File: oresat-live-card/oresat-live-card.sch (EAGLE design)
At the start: 281 parts, among them J1 ORESAT-DEBUG-CONNECTOR-CARD, J100 DM3BT-DSF-PEJS, J102 FTSH-105-XX-X-DV-K, J2 SM06B-SRSS-TB(LF)(SN), J4 TFM-120-01-L-D-RA, Q1 MMBT2907, Q2 PMV45EN, Q3 DMP2240UDM, Q4 PMV45EN, Q5 MOSFET-PCH-SOT23-6, Q6 MOSFET-PCH-SOT23-6, U1 RCLAMP0504FB, U10 TLVH431, U11 TCAN330, U12 MIC842LYC5, U13 MIC842LYC5, U14 MAX4211FETE, U15 TPS62112, U16 MAX7310ATE, U17 25AAXX, U18 RCLAMP0504FB, U2 TPS2051CDBVR, U3 THGBMJG7C2LBAU8, U4 SN74LVC1G07DCK, U7 OSD3358-512M-BSM, Y1 24MHz, Y2 ABS07-32.768KHZ-T

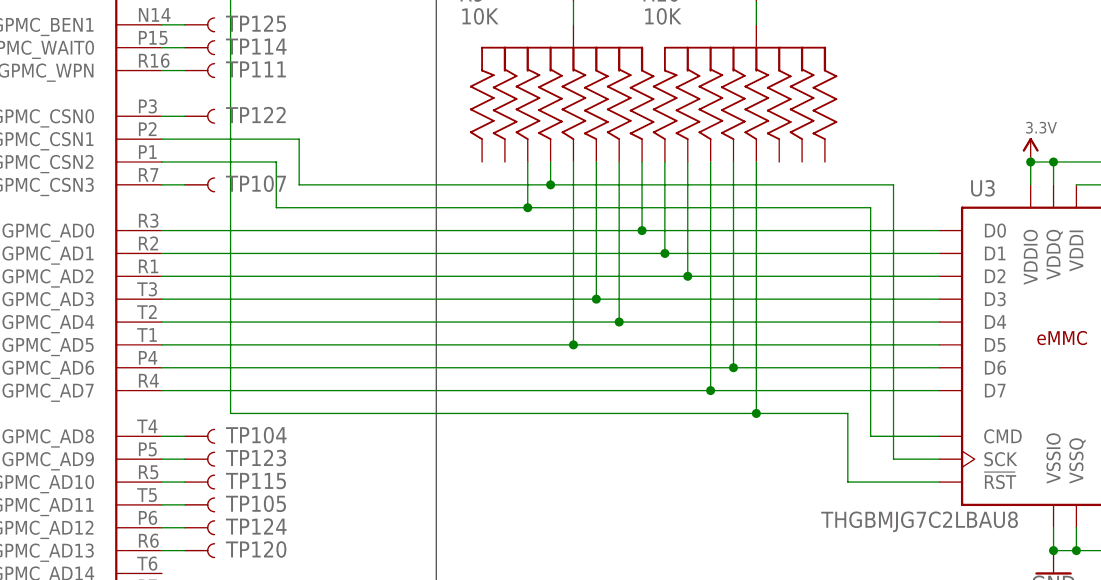
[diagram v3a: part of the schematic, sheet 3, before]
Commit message: relocated emmc pullups and reworked the assigned pins for easier layout
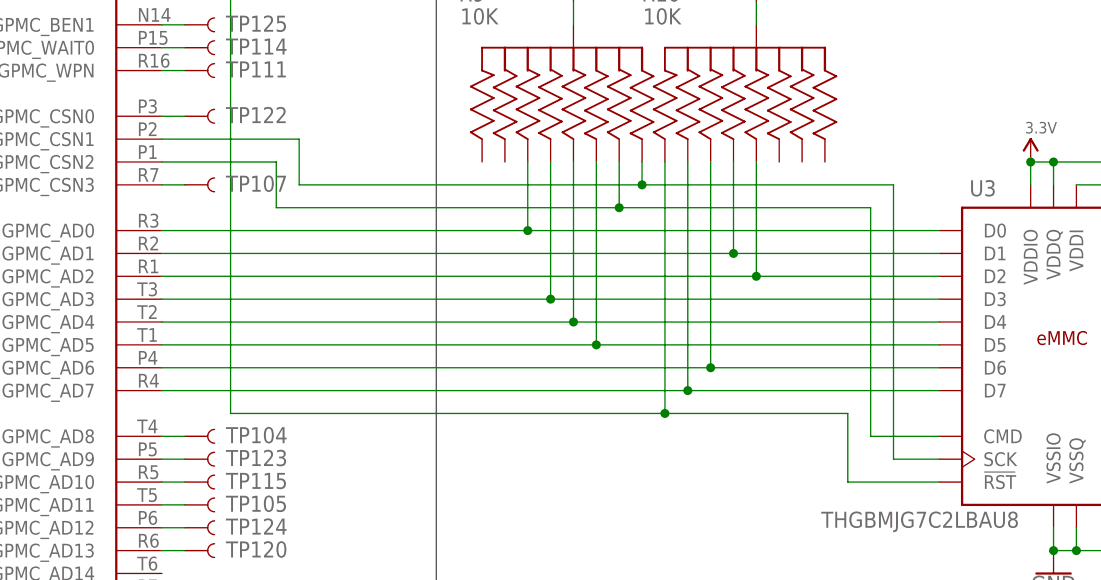
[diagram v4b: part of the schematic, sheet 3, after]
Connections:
- net N$641: now also R9.22; no longer R9.66
- net N$642: now also R10.88; no longer R10.11
- net N$643: now also R10.33; no longer R10.99
- net N$644: now also R9.88; no longer R9.77
- net N$645: now also R9.33; no longer R9.44
- net N$646: now also R9.77; no longer R9.33
- net N$647: now also R10.22; no longer R10.88
- net N$648: now also R10.99; no longer R10.22
- net N$649: now also R9.44; no longer R9.22
- net N$651: now also R9.66; no longer R9.88
- net N$652: now also R10.11; no longer R10.33
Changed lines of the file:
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@@
 <?xml version="1.0" encoding="utf-8"?>
 <!DOCTYPE eagle SYSTEM "eagle.dtd">
-<eagle version="9.6.1">
+<eagle version="9.6.2">
 <drawing>
 <settings>
@@
 <pinref part="U7" gate="C" pin="GPMC_AD0"/>
 <pinref part="U3" gate="U" pin="D0"/>
-<wire x1="350.52" y1="345.44" x2="403.86" y2="345.44" width="0.1524" layer="91"/>
-<wire x1="403.86" y1="345.44" x2="436.88" y2="345.44" width="0.1524" layer="91"/>
-<wire x1="403.86" y1="345.44" x2="403.86" y2="353.06" width="0.1524" layer="91"/>
-<junction x="403.86" y="345.44"/>
-<pinref part="R9" gate="A" pin="66"/>
+<wire x1="350.52" y1="345.44" x2="391.16" y2="345.44" width="0.1524" layer="91"/>
+<pinref part="R9" gate="A" pin="22"/>
+<wire x1="391.16" y1="345.44" x2="436.88" y2="345.44" width="0.1524" layer="91"/>
+<wire x1="391.16" y1="353.06" x2="391.16" y2="345.44" width="0.1524" layer="91"/>
+<junction x="391.16" y="345.44"/>
 </segment>
 </net>
@@
 <pinref part="U7" gate="C" pin="GPMC_AD1"/>
 <pinref part="U3" gate="U" pin="D1"/>
-<wire x1="350.52" y1="342.9" x2="406.4" y2="342.9" width="0.1524" layer="91"/>
-<wire x1="406.4" y1="342.9" x2="436.88" y2="342.9" width="0.1524" layer="91"/>
-<wire x1="406.4" y1="342.9" x2="406.4" y2="353.06" width="0.1524" layer="91"/>
-<junction x="406.4" y="342.9"/>
-<pinref part="R10" gate="A" pin="11"/>
+<wire x1="350.52" y1="342.9" x2="414.02" y2="342.9" width="0.1524" layer="91"/>
+<pinref part="R10" gate="A" pin="88"/>
+<wire x1="414.02" y1="342.9" x2="436.88" y2="342.9" width="0.1524" layer="91"/>
+<wire x1="414.02" y1="353.06" x2="414.02" y2="342.9" width="0.1524" layer="91"/>
+<junction x="414.02" y="342.9"/>
 </segment>
 </net>
@@
 <pinref part="U3" gate="U" pin="D2"/>
 <pinref part="U7" gate="C" pin="GPMC_AD2"/>
-<wire x1="436.88" y1="340.36" x2="408.94" y2="340.36" width="0.1524" layer="91"/>
-<wire x1="408.94" y1="340.36" x2="350.52" y2="340.36" width="0.1524" layer="91"/>
-<wire x1="408.94" y1="340.36" x2="408.94" y2="353.06" width="0.1524" layer="91"/>
-<junction x="408.94" y="340.36"/>
-<pinref part="R10" gate="A" pin="99"/>
+<wire x1="436.88" y1="340.36" x2="416.56" y2="340.36" width="0.1524" layer="91"/>
+<pinref part="R10" gate="A" pin="33"/>
+<wire x1="416.56" y1="340.36" x2="350.52" y2="340.36" width="0.1524" layer="91"/>
+<wire x1="416.56" y1="353.06" x2="416.56" y2="340.36" width="0.1524" layer="91"/>
+<junction x="416.56" y="340.36"/>
 </segment>
 </net>
@@
 <pinref part="U7" gate="C" pin="GPMC_AD3"/>
 <pinref part="U3" gate="U" pin="D3"/>
-<wire x1="350.52" y1="337.82" x2="398.78" y2="337.82" width="0.1524" layer="91"/>
-<wire x1="398.78" y1="337.82" x2="436.88" y2="337.82" width="0.1524" layer="91"/>
-<wire x1="398.78" y1="337.82" x2="398.78" y2="353.06" width="0.1524" layer="91"/>
-<junction x="398.78" y="337.82"/>
-<pinref part="R9" gate="A" pin="77"/>
+<wire x1="350.52" y1="337.82" x2="393.7" y2="337.82" width="0.1524" layer="91"/>
+<pinref part="R9" gate="A" pin="88"/>
+<wire x1="393.7" y1="337.82" x2="436.88" y2="337.82" width="0.1524" layer="91"/>
+<wire x1="393.7" y1="353.06" x2="393.7" y2="337.82" width="0.1524" layer="91"/>
+<junction x="393.7" y="337.82"/>
 </segment>
 </net>
@@
 <pinref part="U3" gate="U" pin="D4"/>
 <pinref part="U7" gate="C" pin="GPMC_AD4"/>
-<wire x1="436.88" y1="335.28" x2="401.32" y2="335.28" width="0.1524" layer="91"/>
-<wire x1="401.32" y1="335.28" x2="350.52" y2="335.28" width="0.1524" layer="91"/>
-<wire x1="401.32" y1="335.28" x2="401.32" y2="353.06" width="0.1524" layer="91"/>
-<junction x="401.32" y="335.28"/>
-<pinref part="R9" gate="A" pin="44"/>
+<wire x1="436.88" y1="335.28" x2="396.24" y2="335.28" width="0.1524" layer="91"/>
+<pinref part="R9" gate="A" pin="33"/>
+<wire x1="396.24" y1="335.28" x2="350.52" y2="335.28" width="0.1524" layer="91"/>
+<wire x1="396.24" y1="353.06" x2="396.24" y2="335.28" width="0.1524" layer="91"/>
+<junction x="396.24" y="335.28"/>
 </segment>
 </net>
@@
 <pinref part="U3" gate="U" pin="D5"/>
 <pinref part="U7" gate="C" pin="GPMC_AD5"/>
-<wire x1="436.88" y1="332.74" x2="396.24" y2="332.74" width="0.1524" layer="91"/>
-<wire x1="396.24" y1="332.74" x2="350.52" y2="332.74" width="0.1524" layer="91"/>
-<wire x1="396.24" y1="332.74" x2="396.24" y2="353.06" width="0.1524" layer="91"/>
-<junction x="396.24" y="332.74"/>
-<pinref part="R9" gate="A" pin="33"/>
+<wire x1="436.88" y1="332.74" x2="398.78" y2="332.74" width="0.1524" layer="91"/>
+<pinref part="R9" gate="A" pin="77"/>
+<wire x1="398.78" y1="332.74" x2="350.52" y2="332.74" width="0.1524" layer="91"/>
+<wire x1="398.78" y1="353.06" x2="398.78" y2="332.74" width="0.1524" layer="91"/>
+<junction x="398.78" y="332.74"/>
 </segment>
 </net>
@@
 <pinref part="U7" gate="C" pin="GPMC_AD6"/>
 <pinref part="U3" gate="U" pin="D6"/>
-<wire x1="350.52" y1="330.2" x2="414.02" y2="330.2" width="0.1524" layer="91"/>
-<wire x1="414.02" y1="330.2" x2="436.88" y2="330.2" width="0.1524" layer="91"/>
-<wire x1="414.02" y1="330.2" x2="414.02" y2="353.06" width="0.1524" layer="91"/>
-<junction x="414.02" y="330.2"/>
-<pinref part="R10" gate="A" pin="88"/>
+<wire x1="350.52" y1="330.2" x2="411.48" y2="330.2" width="0.1524" layer="91"/>
+<pinref part="R10" gate="A" pin="22"/>
+<wire x1="411.48" y1="330.2" x2="436.88" y2="330.2" width="0.1524" layer="91"/>
+<wire x1="411.48" y1="353.06" x2="411.48" y2="330.2" width="0.1524" layer="91"/>
+<junction x="411.48" y="330.2"/>
 </segment>
 </net>
@@
 <pinref part="U3" gate="U" pin="D7"/>
 <pinref part="U7" gate="C" pin="GPMC_AD7"/>
-<wire x1="436.88" y1="327.66" x2="411.48" y2="327.66" width="0.1524" layer="91"/>
-<wire x1="411.48" y1="327.66" x2="350.52" y2="327.66" width="0.1524" layer="91"/>
-<wire x1="411.48" y1="353.06" x2="411.48" y2="327.66" width="0.1524" layer="91"/>
-<junction x="411.48" y="327.66"/>
-<pinref part="R10" gate="A" pin="22"/>
+<wire x1="436.88" y1="327.66" x2="408.94" y2="327.66" width="0.1524" layer="91"/>
+<pinref part="R10" gate="A" pin="99"/>
+<wire x1="408.94" y1="327.66" x2="350.52" y2="327.66" width="0.1524" layer="91"/>
+<wire x1="408.94" y1="353.06" x2="408.94" y2="327.66" width="0.1524" layer="91"/>
+<junction x="408.94" y="327.66"/>
 </segment>
 </net>
@@
 <wire x1="363.22" y1="353.06" x2="363.22" y2="347.98" width="0.1524" layer="91"/>
 <pinref part="U3" gate="U" pin="CMD"/>
-<wire x1="363.22" y1="347.98" x2="391.16" y2="347.98" width="0.1524" layer="91"/>
-<wire x1="391.16" y1="347.98" x2="429.26" y2="347.98" width="0.1524" layer="91"/>
+<wire x1="363.22" y1="347.98" x2="401.32" y2="347.98" width="0.1524" layer="91"/>
+<wire x1="401.32" y1="347.98" x2="429.26" y2="347.98" width="0.1524" layer="91"/>
 <wire x1="436.88" y1="322.58" x2="429.26" y2="322.58" width="0.1524" layer="91"/>
 <wire x1="429.26" y1="322.58" x2="429.26" y2="347.98" width="0.1524" layer="91"/>
-<wire x1="391.16" y1="347.98" x2="391.16" y2="353.06" width="0.1524" layer="91"/>
-<junction x="391.16" y="347.98"/>
-<pinref part="R9" gate="A" pin="22"/>
+<pinref part="R9" gate="A" pin="44"/>
+<wire x1="401.32" y1="353.06" x2="401.32" y2="347.98" width="0.1524" layer="91"/>
+<junction x="401.32" y="347.98"/>
 </segment>
 </net>
@@
 <wire x1="350.52" y1="355.6" x2="365.76" y2="355.6" width="0.1524" layer="91"/>
 <wire x1="365.76" y1="355.6" x2="365.76" y2="350.52" width="0.1524" layer="91"/>
-<wire x1="365.76" y1="350.52" x2="393.7" y2="350.52" width="0.1524" layer="91"/>
-<wire x1="393.7" y1="350.52" x2="431.8" y2="350.52" width="0.1524" layer="91"/>
-<wire x1="393.7" y1="350.52" x2="393.7" y2="353.06" width="0.1524" layer="91"/>
-<junction x="393.7" y="350.52"/>
-<pinref part="R9" gate="A" pin="88"/>
+<wire x1="365.76" y1="350.52" x2="403.86" y2="350.52" width="0.1524" layer="91"/>
+<pinref part="R9" gate="A" pin="66"/>
+<wire x1="403.86" y1="350.52" x2="431.8" y2="350.52" width="0.1524" layer="91"/>
+<wire x1="403.86" y1="353.06" x2="403.86" y2="350.52" width="0.1524" layer="91"/>
+<junction x="403.86" y="350.52"/>
 </segment>
 </net>
@@
 <wire x1="350.52" y1="391.16" x2="358.14" y2="391.16" width="0.1524" layer="91"/>
 <wire x1="358.14" y1="391.16" x2="358.14" y2="325.12" width="0.1524" layer="91"/>
-<wire x1="358.14" y1="325.12" x2="416.56" y2="325.12" width="0.1524" layer="91"/>
+<wire x1="358.14" y1="325.12" x2="406.4" y2="325.12" width="0.1524" layer="91"/>
 <pinref part="U3" gate="U" pin="!RST!"/>
-<wire x1="416.56" y1="325.12" x2="426.72" y2="325.12" width="0.1524" layer="91"/>
+<wire x1="406.4" y1="325.12" x2="426.72" y2="325.12" width="0.1524" layer="91"/>
 <wire x1="436.88" y1="317.5" x2="426.72" y2="317.5" width="0.1524" layer="91"/>
 <wire x1="426.72" y1="317.5" x2="426.72" y2="325.12" width="0.1524" layer="91"/>
-<wire x1="416.56" y1="353.06" x2="416.56" y2="325.12" width="0.1524" layer="91"/>
-<junction x="416.56" y="325.12"/>
-<pinref part="R10" gate="A" pin="33"/>
+<pinref part="R10" gate="A" pin="11"/>
+<wire x1="406.4" y1="353.06" x2="406.4" y2="325.12" width="0.1524" layer="91"/>
+<junction x="406.4" y="325.12"/>
 </segment>
 </net>

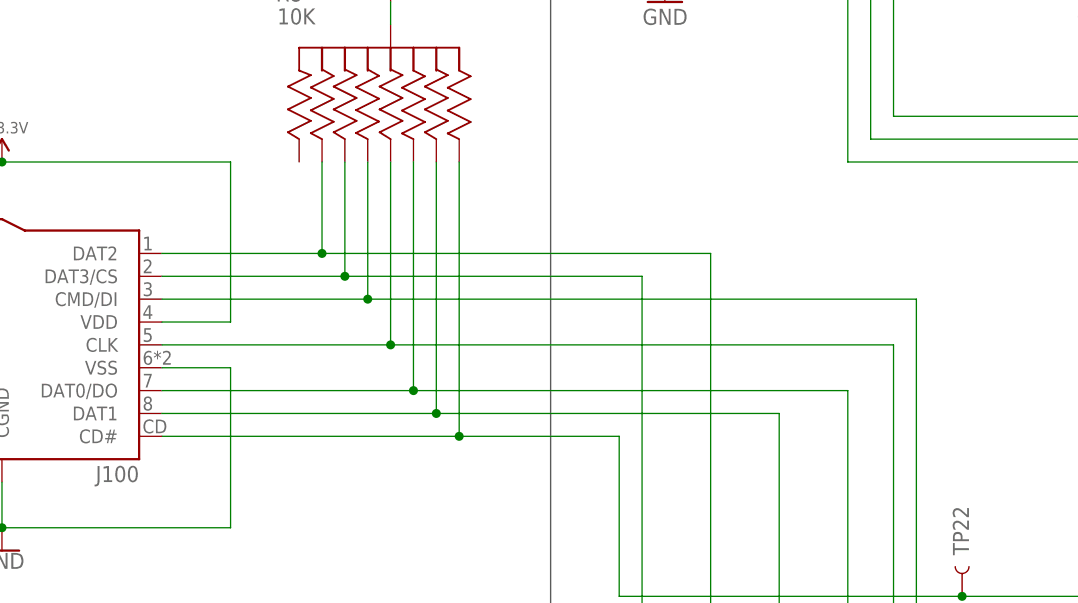
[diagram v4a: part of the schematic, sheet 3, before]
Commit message: routed sd data and reworked R8 pinout
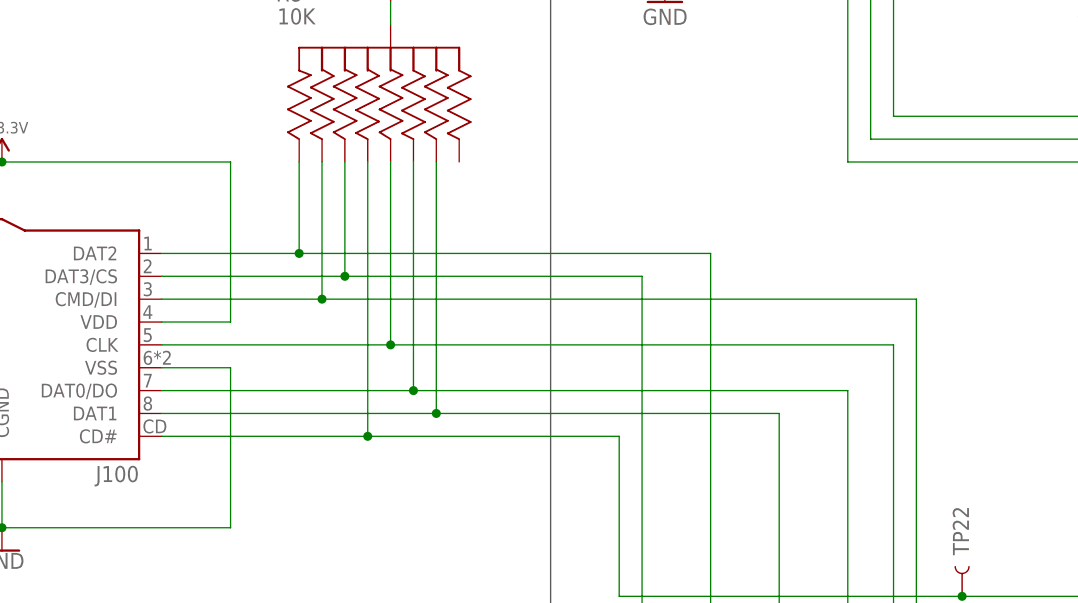
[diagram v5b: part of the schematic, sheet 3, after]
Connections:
- net N$10: now also R8.88; no longer R8.66
- net N$4: now also R8.11; no longer R8.99
- net N$6: now also R8.99; no longer R8.88
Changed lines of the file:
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@@
 <segment>
 <pinref part="J100" gate="G$1" pin="DAT2"/>
-<wire x1="106.68" y1="403.86" x2="124.46" y2="403.86" width="0.1524" layer="91"/>
-<pinref part="R8" gate="A" pin="99"/>
-<wire x1="124.46" y1="403.86" x2="124.46" y2="414.02" width="0.1524" layer="91"/>
-<junction x="124.46" y="403.86"/>
 <pinref part="JP103" gate="G$1" pin="3"/>
 <wire x1="167.64" y1="342.9" x2="167.64" y2="403.86" width="0.1524" layer="91"/>
-<wire x1="167.64" y1="403.86" x2="124.46" y2="403.86" width="0.1524" layer="91"/>
+<wire x1="167.64" y1="403.86" x2="121.92" y2="403.86" width="0.1524" layer="91"/>
+<pinref part="R8" gate="A" pin="11"/>
+<wire x1="121.92" y1="403.86" x2="106.68" y2="403.86" width="0.1524" layer="91"/>
+<wire x1="121.92" y1="414.02" x2="121.92" y2="403.86" width="0.1524" layer="91"/>
+<junction x="121.92" y="403.86"/>
 </segment>
 </net>
@@
 <segment>
 <pinref part="J100" gate="G$1" pin="DAT3/CS"/>
-<pinref part="R8" gate="A" pin="22"/>
-<wire x1="106.68" y1="401.32" x2="127" y2="401.32" width="0.1524" layer="91"/>
-<wire x1="127" y1="401.32" x2="127" y2="414.02" width="0.1524" layer="91"/>
-<junction x="127" y="401.32"/>
 <pinref part="JP102" gate="G$1" pin="3"/>
 <wire x1="160.02" y1="335.28" x2="160.02" y2="401.32" width="0.1524" layer="91"/>
 <wire x1="160.02" y1="401.32" x2="127" y2="401.32" width="0.1524" layer="91"/>
+<pinref part="R8" gate="A" pin="22"/>
+<wire x1="127" y1="401.32" x2="106.68" y2="401.32" width="0.1524" layer="91"/>
+<wire x1="127" y1="414.02" x2="127" y2="401.32" width="0.1524" layer="91"/>
+<junction x="127" y="401.32"/>
 </segment>
 </net>
@@
 <segment>
 <pinref part="J100" gate="G$1" pin="CMD/DI"/>
-<pinref part="R8" gate="A" pin="88"/>
-<wire x1="106.68" y1="398.78" x2="129.54" y2="398.78" width="0.1524" layer="91"/>
-<wire x1="129.54" y1="398.78" x2="129.54" y2="414.02" width="0.1524" layer="91"/>
-<wire x1="129.54" y1="398.78" x2="190.5" y2="398.78" width="0.1524" layer="91"/>
+<wire x1="106.68" y1="398.78" x2="124.46" y2="398.78" width="0.1524" layer="91"/>
+<wire x1="124.46" y1="398.78" x2="190.5" y2="398.78" width="0.1524" layer="91"/>
 <wire x1="190.5" y1="398.78" x2="190.5" y2="355.6" width="0.1524" layer="91"/>
-<junction x="129.54" y="398.78"/>
 <pinref part="U7" gate="C" pin="MMC0_CMD"/>
 <wire x1="190.5" y1="355.6" x2="289.56" y2="355.6" width="0.1524" layer="91"/>
+<pinref part="R8" gate="A" pin="99"/>
+<wire x1="124.46" y1="414.02" x2="124.46" y2="398.78" width="0.1524" layer="91"/>
+<junction x="124.46" y="398.78"/>
 </segment>
 </net>
@@
 <segment>
 <pinref part="J100" gate="G$1" pin="CLK"/>
-<pinref part="R8" gate="A" pin="33"/>
 <wire x1="106.68" y1="393.7" x2="132.08" y2="393.7" width="0.1524" layer="91"/>
-<wire x1="132.08" y1="393.7" x2="132.08" y2="414.02" width="0.1524" layer="91"/>
 <wire x1="132.08" y1="393.7" x2="187.96" y2="393.7" width="0.1524" layer="91"/>
 <wire x1="187.96" y1="393.7" x2="187.96" y2="358.14" width="0.1524" layer="91"/>
-<junction x="132.08" y="393.7"/>
 <pinref part="U7" gate="C" pin="MMC0_CLK"/>
 <wire x1="187.96" y1="358.14" x2="289.56" y2="358.14" width="0.1524" layer="91"/>
+<pinref part="R8" gate="A" pin="33"/>
+<wire x1="132.08" y1="414.02" x2="132.08" y2="393.7" width="0.1524" layer="91"/>
+<junction x="132.08" y="393.7"/>
 </segment>
 </net>
@@
 <segment>
 <pinref part="J100" gate="G$1" pin="DAT0/DO"/>
-<pinref part="R8" gate="A" pin="77"/>
+<pinref part="JP111" gate="G$1" pin="3"/>
 <wire x1="106.68" y1="388.62" x2="134.62" y2="388.62" width="0.1524" layer="91"/>
-<wire x1="134.62" y1="388.62" x2="134.62" y2="414.02" width="0.1524" layer="91"/>
-<junction x="134.62" y="388.62"/>
-<pinref part="JP111" gate="G$1" pin="3"/>
 <wire x1="134.62" y1="388.62" x2="182.88" y2="388.62" width="0.1524" layer="91"/>
 <wire x1="182.88" y1="388.62" x2="182.88" y2="358.14" width="0.1524" layer="91"/>
+<pinref part="R8" gate="A" pin="77"/>
+<wire x1="134.62" y1="414.02" x2="134.62" y2="388.62" width="0.1524" layer="91"/>
+<junction x="134.62" y="388.62"/>
 </segment>
 </net>
@@
 <segment>
 <pinref part="J100" gate="G$1" pin="DAT1"/>
-<pinref part="R8" gate="A" pin="44"/>
-<wire x1="106.68" y1="386.08" x2="137.16" y2="386.08" width="0.1524" layer="91"/>
-<wire x1="137.16" y1="386.08" x2="137.16" y2="414.02" width="0.1524" layer="91"/>
-<junction x="137.16" y="386.08"/>
 <pinref part="JP110" gate="G$1" pin="3"/>
 <wire x1="175.26" y1="350.52" x2="175.26" y2="386.08" width="0.1524" layer="91"/>
 <wire x1="175.26" y1="386.08" x2="137.16" y2="386.08" width="0.1524" layer="91"/>
+<pinref part="R8" gate="A" pin="44"/>
+<wire x1="137.16" y1="386.08" x2="106.68" y2="386.08" width="0.1524" layer="91"/>
+<wire x1="137.16" y1="414.02" x2="137.16" y2="386.08" width="0.1524" layer="91"/>
+<junction x="137.16" y="386.08"/>
 </segment>
 </net>
@@
 <segment>
 <pinref part="J100" gate="G$1" pin="CD#"/>
-<pinref part="R8" gate="A" pin="66"/>
-<wire x1="106.68" y1="383.54" x2="139.7" y2="383.54" width="0.1524" layer="91"/>
-<wire x1="139.7" y1="383.54" x2="139.7" y2="414.02" width="0.1524" layer="91"/>
-<wire x1="139.7" y1="383.54" x2="157.48" y2="383.54" width="0.1524" layer="91"/>
-<junction x="139.7" y="383.54"/>
+<wire x1="106.68" y1="383.54" x2="129.54" y2="383.54" width="0.1524" layer="91"/>
 <pinref part="TP22" gate="G$1" pin="1"/>
 <pinref part="U7" gate="C" pin="SPI0_CS1"/>
+<wire x1="129.54" y1="383.54" x2="157.48" y2="383.54" width="0.1524" layer="91"/>
 <wire x1="195.58" y1="365.76" x2="289.56" y2="365.76" width="0.1524" layer="91"/>
 <wire x1="157.48" y1="383.54" x2="157.48" y2="365.76" width="0.1524" layer="91"/>
 <wire x1="157.48" y1="365.76" x2="195.58" y2="365.76" width="0.1524" layer="91"/>
 <junction x="195.58" y="365.76"/>
+<pinref part="R8" gate="A" pin="88"/>
+<wire x1="129.54" y1="414.02" x2="129.54" y2="383.54" width="0.1524" layer="91"/>
+<junction x="129.54" y="383.54"/>
 </segment>
 </net>
